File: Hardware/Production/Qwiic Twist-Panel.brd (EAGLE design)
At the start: 81.5 x 97.3 mm, 363 parts, among them J12 ISP, J14 PTH, J18 ISP, J20 PTH, J24 ISP, J26 PTH, J3 PTH, J30 ISP, J32 PTH, J36 ISP, J6 PTH, J7 ISP, SW1 Rotary Encoder, SW2 Rotary Encoder, SW3 Rotary Encoder, SW4 Rotary Encoder, SW5 Rotary Encoder, SW6 Rotary Encoder, U1 ATTINY84-ARDUINO, U2 ATTINY84-ARDUINO, U3 ATTINY84-ARDUINO, U4 ATTINY84-ARDUINO, U5 ATTINY84-ARDUINO, U6 ATTINY84-ARDUINO

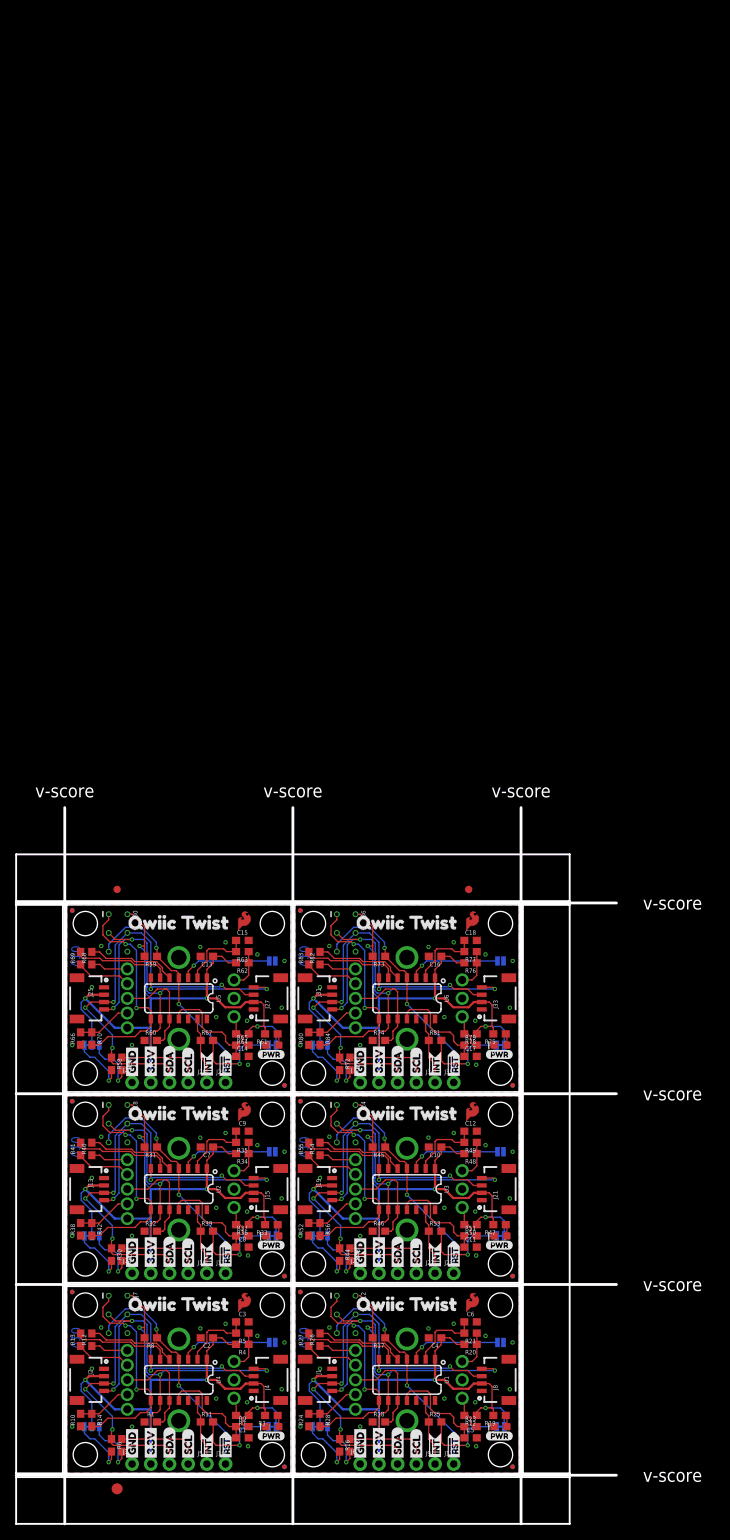
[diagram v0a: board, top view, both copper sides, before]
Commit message: Increasing panel size for better production.
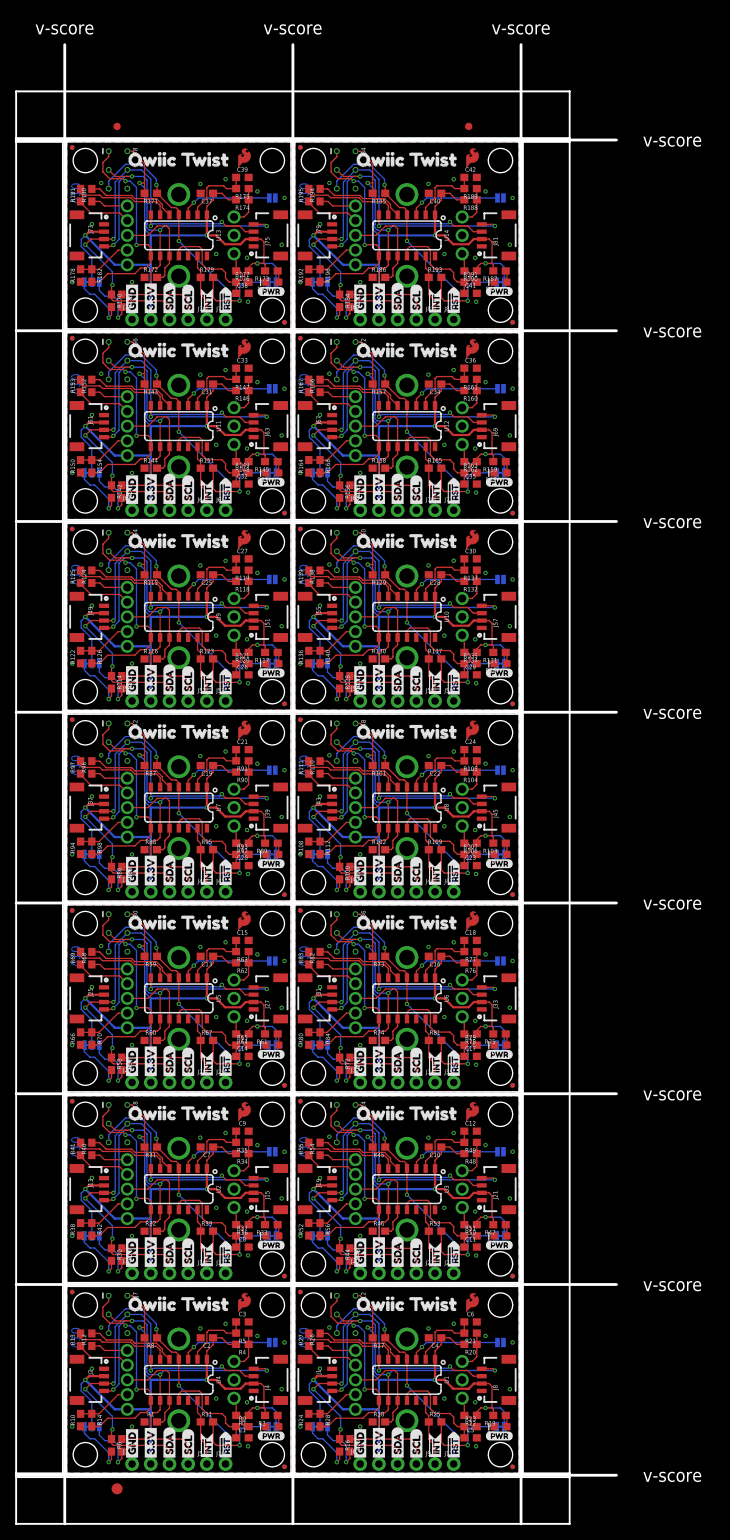
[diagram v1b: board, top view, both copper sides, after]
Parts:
- added C19, C22, C25, C28, C31, C34, C37, C40: 0.1uF, SparkFun-Capacitors:0603
- added C20, C21, C23, C24, C26, C27, C29, C30, C32, C33, C35, C36, C38, C39, C41, C42: 10nF, SparkFun-Capacitors:0603
- added D10, D11, D12, D13, D14, D7, D8, D9: RED, SparkFun-LED:LED-0603
- added INT10, INT11, INT12, INT13, INT6, INT7, INT8, INT9: (no value), SparkFun-Jumpers:SMT-JUMPER_2_NC_TRACE_SILK
- added J37, J39, J43, J45, J49, J51, J55, J57, J61, J63, J67, J69, J73, J75, J79, J81: (no value), SparkFun-Connectors:1X04_1MM_RA
- added J38, J44, J50, J56, J62, J68, J74, J80: PTH, SparkX:1X04_NO_SILK
- added J40, J41, J46, J47, J52, J53, J58, J59, J64, J65, J70, J71, J76, J77, J82, J83: (no value), SparkFun-Connectors:1X01_NO_SILK
- added J42, J48, J54, J60, J66, J72, J78, J84: ISP, SparkFun-Connectors:2X3_TEST_POINTS
- added JP100, JP103, JP104, JP105, JP110, JP113, JP114, JP115, JP120, JP123, JP124, JP125, JP130, JP133, JP134, JP135, JP140, JP63, JP64, JP65, JP70, JP73, JP74, JP75, JP80, JP83, JP84, JP85, JP90, JP93, JP94, JP95: FIDUCIALUFIDUCIAL, SparkFun:MICRO-FIDUCIAL
- added JP101, JP102, JP108, JP109, JP111, JP112, JP118, JP119, JP121, JP122, JP128, JP129, JP131, JP132, JP138, JP139, JP61, JP62, JP68, JP69, JP71, JP72, JP78, JP79, JP81, JP82, JP88, JP89, JP91, JP92, JP98, JP99: STAND-OFF, SparkFun:STAND-OFF
- added JP106, JP116, JP126, JP136, JP66, JP76, JP86, JP96: ADR, SparkFun-Jumpers:SMT-JUMPER_2_NO_SILK
- added JP107, JP117, JP127, JP137, JP67, JP77, JP87, JP97: (no value), SparkFun-Jumpers:SMT-JUMPER_3_2-NC_TRACE_SILK
- added LOGO19, LOGO22, LOGO25, LOGO28, LOGO31, LOGO34, LOGO37, LOGO40: OSHW-LOGOMINI, SparkFun-Aesthetics:OSHW-LOGO-MINI
- added LOGO20, LOGO23, LOGO26, LOGO29, LOGO32, LOGO35, LOGO38, LOGO41: SFE_LOGO_NAME_FLAME.1_INCH, SparkFun-Aesthetics:SFE_LOGO_NAME_FLAME_.1
- added LOGO21, LOGO24, LOGO27, LOGO30, LOGO33, LOGO36, LOGO39, LOGO42: SFE_LOGO_FLAME.1EXP, SparkFun-Aesthetics:SFE_LOGO_FLAME_COPPER_EXPOSED_.1
- added R100, R113, R114, R127, R128, R141, R142, R155, R156, R169, R170, R183, R184, R85, R86, R99: 2.2k, SparkFun-Resistors:0603
- added R101, R102, R104, R105, R106, R107, R109, R115, R116, R118, R119, R120, R121, R123, R129, R130, R132, R133, R134, R135, R137, R143, R144, R146, R147, R148, R149, R151, R157, R158, R160, R161, R162, R163, R165, R171, R172, R174, R175, R176, R177, R179, R185, R186, R188, R189, R190, R191, R193, R87, R88, R90, R91, R92, R93, R95: 10k, SparkFun-Resistors:0603
- added R103, R117, R131, R145, R159, R173, R187, R89: 1k, SparkFun-Resistors:0603
- added R108, R122, R136, R150, R164, R178, R192, R94: DNP, SparkFun-Resistors:0603
- added R110, R111, R112, R124, R125, R126, R138, R139, R140, R152, R153, R154, R166, R167, R168, R180, R181, R182, R194, R195, R196, R96, R97, R98: 10, SparkFun-Resistors:0603
- added SW10, SW11, SW12, SW13, SW14, SW7, SW8, SW9: Rotary Encoder, SparkFun-Switches:ENCODER_LED_3_KIT
- added U$121, U$126, U$141, U$146, U$161, U$166, U$181, U$186, U$201, U$206, U$221, U$226, U$241, U$246, U$261, U$266: (no value), Labels-0_04:3#3V2
- added U$122, U$125, U$142, U$145, U$162, U$165, U$182, U$185, U$202, U$205, U$222, U$225, U$242, U$245, U$262, U$265: (no value), Labels-0_04:GND1
- added U$123, U$128, U$143, U$148, U$163, U$168, U$183, U$188, U$203, U$208, U$223, U$228, U$243, U$248, U$263, U$268: (no value), Labels-0_04:SCL9
- added U$124, U$127, U$144, U$147, U$164, U$167, U$184, U$187, U$204, U$207, U$224, U$227, U$244, U$247, U$264, U$267: (no value), Labels-0_04:SDA8
- added U$129, U$149, U$169, U$189, U$209, U$229, U$249, U$269: (no value), Labels:I_SUPER2_C-()-03
- added U$130, U$131, U$150, U$151, U$170, U$171, U$190, U$191, U$210, U$211, U$230, U$231, U$250, U$251, U$270, U$271: (no value), Labels:INT#-[<
- added U$132, U$133, U$152, U$153, U$172, U$173, U$192, U$193, U$212, U$213, U$232, U$233, U$252, U$253, U$272, U$273: (no value), Labels:RST#-[>
- added U$134, U$154, U$174, U$194, U$214, U$234, U$254, U$274: (no value), Labels:PWR-()-03
- added U$135, U$155, U$175, U$195, U$215, U$235, U$255, U$275: (no value), Labels:ADR-()-03
- added U$136, U$156, U$176, U$196, U$216, U$236, U$256, U$276: (no value), Labels:QWIIC-LOGO-MEDIUM
- added U$137, U$157, U$177, U$197, U$217, U$237, U$257, U$277: (no value), buzzard_labels (53):QWIIC1
- added U$138, U$158, U$178, U$198, U$218, U$238, U$258, U$278: (no value), buzzard_labels (53):TWIST2
- added U$139, U$159, U$179, U$199, U$219, U$239, U$259, U$279: (no value), buzzard_labels (54):QWIIC_TWIST1
- added U$140, U$160, U$180, U$200, U$220, U$240, U$260, U$280: (no value), buzzard_labels (56):INT0
- added U10, U11, U12, U13, U14, U7, U8, U9: ATTINY84-ARDUINO, SparkFun-IC-Microcontroller:SO14
- R12, R13, R14, R26, R27, R28, R40, R41, R42, R54, R55, R56, R68, R69, R70, R82, R83, R84: value 100 -> 10
- SW1, SW2, SW3, SW4, SW5, SW6: device SparkFun-Electromechanical:ENCODER_LED_3_KIT -> SparkFun-Switches:ENCODER_LED_3_KIT
- moved E$1 103.6 mm to (6.86, 182.9)
- moved E$2 103.6 mm to (54.6, 182.9)
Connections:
- new net !INT10: J64.1, R151.1, U11.13
- new net !INT11: J70.1, R165.1, U12.13
- new net !INT12: J76.1, R179.1, U13.13
- new net !INT13: J82.1, R193.1, U14.13
- new net !INT6: J40.1, R95.1, U7.13
- new net !INT7: J46.1, R109.1, U8.13
- new net !INT8: J52.1, R123.1, U9.13
- new net !INT9: J58.1, R137.1, U10.13
- new net !RST10: J65.1, J66.5, R143.1, U11.4
- new net !RST11: J71.1, J72.5, R157.1, U12.4
- new net !RST12: J77.1, J78.5, R171.1, U13.4
- new net !RST13: J83.1, J84.5, R185.1, U14.4
- new net !RST6: J41.1, J42.5, R87.1, U7.4
- new net !RST7: J47.1, J48.5, R101.1, U8.4
- new net !RST8: J53.1, J54.5, R115.1, U9.4
- new net !RST9: J59.1, J60.5, R129.1, U10.4
- new net 3.3V10: C31.1, INT10.2, J61.2, J62.2, J63.2, J66.2, JP107.2, R143.2, R145.2, R146.2, R148.1, SW11.5, U11.1
- new net 3.3V11: C34.1, INT11.2, J67.2, J68.2, J69.2, J72.2, JP117.2, R157.2, R159.2, R160.2, R162.1, SW12.5, U12.1
- new net 3.3V12: C37.1, INT12.2, J73.2, J74.2, J75.2, J78.2, JP127.2, R171.2, R173.2, R174.2, R176.1, SW13.5, U13.1
- new net 3.3V13: C40.1, INT13.2, J79.2, J80.2, J81.2, J84.2, JP137.2, R185.2, R187.2, R188.2, R190.1, SW14.5, U14.1
- new net 3.3V6: C19.1, INT6.2, J37.2, J38.2, J39.2, J42.2, JP67.2, R87.2, R89.2, R90.2, R92.1, SW7.5, U7.1
- new net 3.3V7: C22.1, INT7.2, J43.2, J44.2, J45.2, J48.2, JP77.2, R101.2, R103.2, R104.2, R106.1, SW8.5, U8.1
- new net 3.3V8: C25.1, INT8.2, J49.2, J50.2, J51.2, J54.2, JP87.2, R115.2, R117.2, R118.2, R120.1, SW9.5, U9.1
- new net 3.3V9: C28.1, INT9.2, J55.2, J56.2, J57.2, J60.2, JP97.2, R129.2, R131.2, R132.2, R134.1, SW10.5, U10.1
- new net A10: R146.1, R147.1, SW11.A
- new net A11: R160.1, R161.1, SW12.A
- new net A12: R174.1, R175.1, SW13.A
- new net A13: R188.1, R189.1, SW14.A
- new net A6: R90.1, R91.1, SW7.A
- new net A7: R104.1, R105.1, SW8.A
- new net A8: R118.1, R119.1, SW9.A
- new net A9: R132.1, R133.1, SW10.A
- new net ADR10: JP106.2, U11.3
- new net ADR11: JP116.2, U12.3
- new net ADR12: JP126.2, U13.3
- new net ADR13: JP136.2, U14.3
- new net ADR6: JP66.2, U7.3
- new net ADR7: JP76.2, U8.3
- new net ADR8: JP86.2, U9.3
- new net ADR9: JP96.2, U10.3
- new net B10: R148.2, R149.2, SW11.B
- new net B11: R162.2, R163.2, SW12.B
- new net B12: R176.2, R177.2, SW13.B
- new net B13: R190.2, R191.2, SW14.B
- new net B6: R92.2, R93.2, SW7.B
- new net B7: R106.2, R107.2, SW8.B
- new net B8: R120.2, R121.2, SW9.B
- new net B9: R134.2, R135.2, SW10.B
- new net BLUE10: J66.1, R154.2, U11.8
- new net BLUE11: J72.1, R168.2, U12.8
- new net BLUE12: J78.1, R182.2, U13.8
- new net BLUE13: J84.1, R196.2, U14.8
- new net BLUE6: J42.1, R98.2, U7.8
- new net BLUE7: J48.1, R112.2, U8.8
- new net BLUE8: J54.1, R126.2, U9.8
- new net BLUE9: J60.1, R140.2, U10.8
- new net BLUE_RAW10: R150.2, R154.1, SW11.4
- new net BLUE_RAW11: R164.2, R168.1, SW12.4
- new net BLUE_RAW12: R178.2, R182.1, SW13.4
- new net BLUE_RAW13: R192.2, R196.1, SW14.4
- new net BLUE_RAW6: R94.2, R98.1, SW7.4
- new net BLUE_RAW7: R108.2, R112.1, SW8.4
- new net BLUE_RAW8: R122.2, R126.1, SW9.4
- new net BLUE_RAW9: R136.2, R140.1, SW10.4
- new net ENCODER_A10: C33.1, R147.2, U11.2
- new net ENCODER_A11: C36.1, R161.2, U12.2
- new net ENCODER_A12: C39.1, R175.2, U13.2
- new net ENCODER_A13: C42.1, R189.2, U14.2
- new net ENCODER_A6: C21.1, R91.2, U7.2
- new net ENCODER_A7: C24.1, R105.2, U8.2
- new net ENCODER_A8: C27.1, R119.2, U9.2
- new net ENCODER_A9: C30.1, R133.2, U10.2
- new net ENCODER_B10: C32.1, R149.1, U11.11
- new net ENCODER_B11: C35.1, R163.1, U12.11
- new net ENCODER_B12: C38.1, R177.1, U13.11
- new net ENCODER_B13: C41.1, R191.1, U14.11
- new net ENCODER_B6: C20.1, R93.1, U7.11
- new net ENCODER_B7: C23.1, R107.1, U8.11
- new net ENCODER_B8: C26.1, R121.1, U9.11
- new net ENCODER_B9: C29.1, R135.1, U10.11
- new net GND10: C31.2, C32.2, C33.2, D11.C, J61.1, J62.1, J63.1, J66.6, JP106.1, R144.1, R150.1, SW11.C, U11.14
- new net GND11: C34.2, C35.2, C36.2, D12.C, J67.1, J68.1, J69.1, J72.6, JP116.1, R158.1, R164.1, SW12.C, U12.14
- new net GND12: C37.2, C38.2, C39.2, D13.C, J73.1, J74.1, J75.1, J78.6, JP126.1, R172.1, R178.1, SW13.C, U13.14
- new net GND13: C40.2, C41.2, C42.2, D14.C, J79.1, J80.1, J81.1, J84.6, JP136.1, R186.1, R192.1, SW14.C, U14.14
- new net GND6: C19.2, C20.2, C21.2, D7.C, J37.1, J38.1, J39.1, J42.6, JP66.1, R88.1, R94.1, SW7.C, U7.14
- new net GND7: C22.2, C23.2, C24.2, D8.C, J43.1, J44.1, J45.1, J48.6, JP76.1, R102.1, R108.1, SW8.C, U8.14
- new net GND8: C25.2, C26.2, C27.2, D9.C, J49.1, J50.1, J51.1, J54.6, JP86.1, R116.1, R122.1, SW9.C, U9.14
- new net GND9: C28.2, C29.2, C30.2, D10.C, J55.1, J56.1, J57.1, J60.6, JP96.1, R130.1, R136.1, SW10.C, U10.14
- new net GREEN10: R153.2, U11.6
- new net GREEN11: R167.2, U12.6
- new net GREEN12: R181.2, U13.6
- new net GREEN13: R195.2, U14.6
- new net GREEN6: R97.2, U7.6
- new net GREEN7: R111.2, U8.6
- new net GREEN8: R125.2, U9.6
- new net GREEN9: R139.2, U10.6
- new net GREEN_RAW10: R153.1, SW11.2
- new net GREEN_RAW11: R167.1, SW12.2
- new net GREEN_RAW12: R181.1, SW13.2
- new net GREEN_RAW13: R195.1, SW14.2
- new net GREEN_RAW6: R97.1, SW7.2
- new net GREEN_RAW7: R111.1, SW8.2
- new net GREEN_RAW8: R125.1, SW9.2
- new net GREEN_RAW9: R139.1, SW10.2
- new net INT_R10: INT10.1, R151.2
- new net INT_R11: INT11.1, R165.2
- new net INT_R12: INT12.1, R179.2
- new net INT_R13: INT13.1, R193.2
- new net INT_R6: INT6.1, R95.2
- new net INT_R7: INT7.1, R109.2
- new net INT_R8: INT8.1, R123.2
- new net INT_R9: INT9.1, R137.2
- new net N$10: D10.A, R131.1
- new net N$11: D11.A, R145.1
- new net N$12: D12.A, R159.1
- new net N$13: D13.A, R173.1
- new net N$14: D14.A, R187.1
- new net N$7: D7.A, R89.1
- new net N$8: D8.A, R103.1
- new net N$9: D9.A, R117.1
- new net RED10: R152.2, U11.5
- new net RED11: R166.2, U12.5
- new net RED12: R180.2, U13.5
- new net RED13: R194.2, U14.5
- new net RED6: R96.2, U7.5
- new net RED7: R110.2, U8.5
- new net RED8: R124.2, U9.5
- new net RED9: R138.2, U10.5
- new net RED_RAW10: R152.1, SW11.1
- new net RED_RAW11: R166.1, SW12.1
- new net RED_RAW12: R180.1, SW13.1
- new net RED_RAW13: R194.1, SW14.1
- new net RED_RAW6: R96.1, SW7.1
- new net RED_RAW7: R110.1, SW8.1
- new net RED_RAW8: R124.1, SW9.1
- new net RED_RAW9: R138.1, SW10.1
- new net SCL10: J61.4, J62.4, J63.4, J66.3, R141.1, U11.9
- new net SCL11: J67.4, J68.4, J69.4, J72.3, R155.1, U12.9
- new net SCL12: J73.4, J74.4, J75.4, J78.3, R169.1, U13.9
- new net SCL13: J79.4, J80.4, J81.4, J84.3, R183.1, U14.9
- new net SCL6: J37.4, J38.4, J39.4, J42.3, R85.1, U7.9
- new net SCL7: J43.4, J44.4, J45.4, J48.3, R99.1, U8.9
- new net SCL8: J49.4, J50.4, J51.4, J54.3, R113.1, U9.9
- new net SCL9: J55.4, J56.4, J57.4, J60.3, R127.1, U10.9
- new net SCL_PU10: JP97.1, R127.2
- new net SCL_PU11: JP107.1, R141.2
- new net SCL_PU12: JP117.1, R155.2
- new net SCL_PU13: JP127.1, R169.2
- new net SCL_PU14: JP137.1, R183.2
- new net SCL_PU7: JP67.1, R85.2
- new net SCL_PU8: JP77.1, R99.2
- new net SCL_PU9: JP87.1, R113.2
- new net SDA10: J61.3, J62.3, J63.3, J66.4, R142.1, U11.7
- new net SDA11: J67.3, J68.3, J69.3, J72.4, R156.1, U12.7
- new net SDA12: J73.3, J74.3, J75.3, J78.4, R170.1, U13.7
- new net SDA13: J79.3, J80.3, J81.3, J84.4, R184.1, U14.7
- new net SDA6: J37.3, J38.3, J39.3, J42.4, R86.1, U7.7
- new net SDA7: J43.3, J44.3, J45.3, J48.4, R100.1, U8.7
- new net SDA8: J49.3, J50.3, J51.3, J54.4, R114.1, U9.7
- new net SDA9: J55.3, J56.3, J57.3, J60.4, R128.1, U10.7
- new net SDA_PU10: JP97.3, R128.2
- new net SDA_PU11: JP107.3, R142.2
- new net SDA_PU12: JP117.3, R156.2
- new net SDA_PU13: JP127.3, R170.2
- new net SDA_PU14: JP137.3, R184.2
- new net SDA_PU7: JP67.3, R86.2
- new net SDA_PU8: JP77.3, R100.2
- new net SDA_PU9: JP87.3, R114.2
- new net SWITCH10: R144.2, SW11.3, U11.10
- new net SWITCH11: R158.2, SW12.3, U12.10
- new net SWITCH12: R172.2, SW13.3, U13.10
- new net SWITCH13: R186.2, SW14.3, U14.10
- new net SWITCH6: R88.2, SW7.3, U7.10
- new net SWITCH7: R102.2, SW8.3, U8.10
- new net SWITCH8: R116.2, SW9.3, U9.10
- new net SWITCH9: R130.2, SW10.3, U10.10
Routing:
- net 3.3V11: track 0.00 -> 85.0 mm, vias 0 -> 4
- net 3.3V10: track 0.00 -> 85.0 mm, vias 0 -> 4
- net 3.3V7: track 0.00 -> 85.0 mm, vias 0 -> 4
- net 3.3V6: track 0.00 -> 85.0 mm, vias 0 -> 4
- net 3.3V9: track 0.00 -> 85.0 mm, vias 0 -> 4
- net 3.3V8: track 0.00 -> 85.0 mm, vias 0 -> 4
- net 3.3V13: track 0.00 -> 85.0 mm, vias 0 -> 4
- net 3.3V12: track 0.00 -> 85.0 mm, vias 0 -> 4
- net SCL12: track 0.00 -> 64.6 mm, vias 0 -> 4
- net SCL10: track 0.00 -> 64.6 mm, vias 0 -> 4
- net SCL13: track 0.00 -> 64.6 mm, vias 0 -> 4
- net SCL8: track 0.00 -> 64.6 mm, vias 0 -> 4
- net SCL6: track 0.00 -> 64.6 mm, vias 0 -> 4
- net SCL9: track 0.00 -> 64.6 mm, vias 0 -> 4
- net SCL7: track 0.00 -> 64.6 mm, vias 0 -> 4
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- added copper zone on layer 1, net GND10
- added copper zone on layer 16, net GND10
- added copper zone on layer 1, net GND11
- added copper zone on layer 16, net GND11
- added copper zone on layer 1, net GND12
- added copper zone on layer 16, net GND12
- added copper zone on layer 1, net GND13
- added copper zone on layer 16, net GND13
- added copper zone on layer 1, net GND6
- added copper zone on layer 16, net GND6
- added copper zone on layer 1, net GND7
- added copper zone on layer 16, net GND7
- added copper zone on layer 1, net GND8
- added copper zone on layer 16, net GND8
- added copper zone on layer 1, net GND9
- added copper zone on layer 16, net GND9
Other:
- board size 81.5 x 97.3 mm -> 81.5 x 200.9 mm
